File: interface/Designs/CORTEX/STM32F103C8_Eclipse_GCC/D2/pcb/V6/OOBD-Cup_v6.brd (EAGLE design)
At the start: 160 x 100 mm, 55 parts, among them IC1 PCA82C250T, IC2 78L05SMD, IC3 MC34063-SO, IC4 BTM-182, Q1 8MHz, T1 BC817, T2 BC817, T3 BC817, U1 STM32F10XTXU6

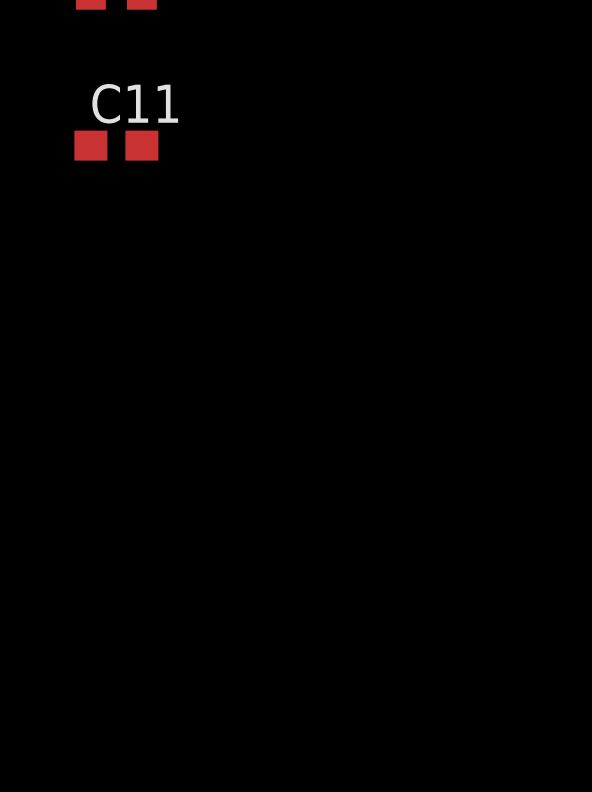
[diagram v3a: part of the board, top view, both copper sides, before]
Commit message: connect Relais to STM32 and add further EMC capacitor
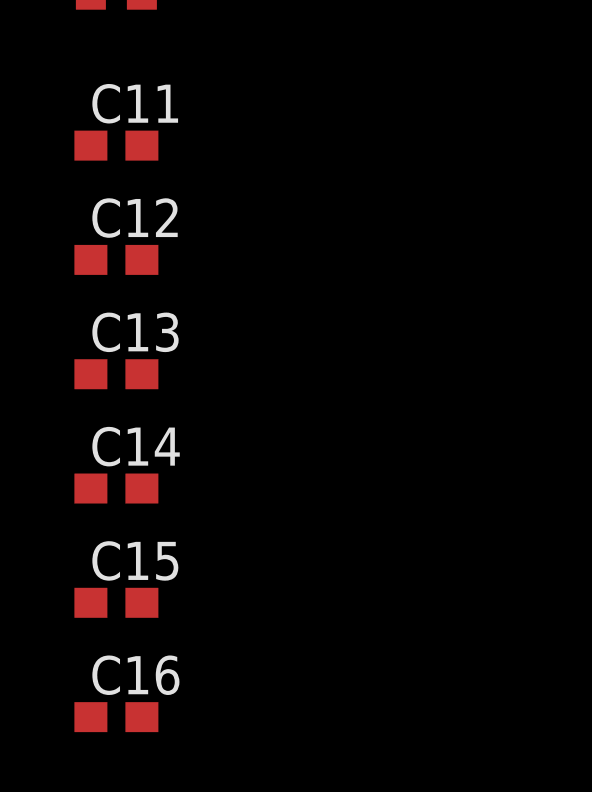
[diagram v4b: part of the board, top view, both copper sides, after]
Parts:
- added C12, C13, C14, C15, C16: 100nF, resistor:C0603
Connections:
- net +3V3: now also C12.1, C13.1, C14.1, C15.1
- net +5V: now also C16.1
- net CAN_SW: now also U1.30
- net GND: now also C12.2, C13.2, C14.2, C15.2, C16.2
- net REL_DIAG: now also U1.16
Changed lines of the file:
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@@
 <element name="R21" library="resistor" package="R0603" value="27k" x="-91.44" y="-153.67"/>
 <element name="C11" library="resistor" package="C0603" value="" x="-91.44" y="-158.75"/>
+<element name="C12" library="resistor" package="C0603" value="100nF" x="-91.44" y="-162.56"/>
+<element name="C13" library="resistor" package="C0603" value="100nF" x="-91.44" y="-166.37"/>
+<element name="C14" library="resistor" package="C0603" value="100nF" x="-91.44" y="-170.18"/>
+<element name="C15" library="resistor" package="C0603" value="100nF" x="-91.44" y="-173.99"/>
+<element name="C16" library="resistor" package="C0603" value="100nF" x="-91.44" y="-177.8"/>
 </elements>
 <signals>
@@
 <contactref element="R21" pad="1"/>
 <contactref element="C11" pad="2"/>
+<contactref element="C13" pad="2"/>
+<contactref element="C14" pad="2"/>
+<contactref element="C12" pad="2"/>
+<contactref element="C15" pad="2"/>
+<contactref element="C16" pad="2"/>
+<wire x1="-90.59" y1="-158.75" x2="-90.59" y2="-162.56" width="0" layer="19" extent="1-1"/>
+<wire x1="-90.59" y1="-166.37" x2="-90.59" y2="-162.56" width="0" layer="19" extent="1-1"/>
+<wire x1="-90.59" y1="-170.18" x2="-90.59" y2="-166.37" width="0" layer="19" extent="1-1"/>
+<wire x1="-90.59" y1="-173.99" x2="-90.59" y2="-170.18" width="0" layer="19" extent="1-1"/>
+<wire x1="-90.59" y1="-177.8" x2="-90.59" y2="-173.99" width="0" layer="19" extent="1-1"/>
 <wire x1="-92.29" y1="-153.67" x2="-90.59" y2="-158.75" width="0" layer="19" extent="1-1"/>
 <wire x1="-92.29" y1="-140.97" x2="-92.29" y2="-153.67" width="0" layer="19" extent="1-1"/>
@@
 <contactref element="R17" pad="2"/>
 <contactref element="JP1" pad="1"/>
+<contactref element="C12" pad="1"/>
+<contactref element="C14" pad="1"/>
+<contactref element="C13" pad="1"/>
+<contactref element="C15" pad="1"/>
+<wire x1="-92.29" y1="-162.56" x2="-90.59" y2="-134.62" width="0" layer="19" extent="1-1"/>
+<wire x1="-92.29" y1="-166.37" x2="-92.29" y2="-162.56" width="0" layer="19" extent="1-1"/>
+<wire x1="-92.29" y1="-170.18" x2="-92.29" y2="-166.37" width="0" layer="19" extent="1-1"/>
+<wire x1="-92.29" y1="-173.99" x2="-92.29" y2="-170.18" width="0" layer="19" extent="1-1"/>
 <wire x1="-72.39" y1="-110.49" x2="-90.59" y2="-134.62" width="0" layer="19" extent="1-1"/>
 <wire x1="-57.15" y1="-111.76" x2="-72.39" y2="-110.49" width="0" layer="19" extent="1-1"/>
@@
 <contactref element="R8" pad="1"/>
 <contactref element="R9" pad="2"/>
+<contactref element="U1" pad="16"/>
 <wire x1="-53.76" y1="-49.53" x2="-66.89" y2="-49.53" width="0" layer="19" extent="1-1"/>
+<wire x1="-28.21" y1="40.48" x2="-53.76" y2="-49.53" width="0" layer="19" extent="1-1"/>
 </signal>
 <signal name="N$20">
@@
 <signal name="CAN_SW">
 <contactref element="R7" pad="1"/>
+<contactref element="U1" pad="30"/>
+<wire x1="-28.21" y1="45.88" x2="-60.54" y2="-49.53" width="0" layer="19" extent="1-1"/>
 </signal>
 <signal name="N$27">
@@
 <contactref element="IC2" pad="1"/>
 <contactref element="C8" pad="1"/>
+<contactref element="C16" pad="1"/>
 <wire x1="-81.915" y1="-110.55" x2="-83.4" y2="-119.38" width="0" layer="19" extent="1-1"/>
 <wire x1="-69.215" y1="-79.2734" x2="-81.915" y2="-110.55" width="0" layer="19" extent="1-1"/>
+<wire x1="-92.29" y1="-177.8" x2="-83.4" y2="-119.38" width="0" layer="19" extent="1-1"/>
 <wire x1="-34.925" y1="2.0066" x2="-69.215" y2="-79.2734" width="0" layer="19" extent="1-1"/>
 </signal>

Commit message: add missing parts and doe last modification for first prototypes/batch
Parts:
- added C17: 47µ/35V, cap-master:SV-D
- added C18: 100nF, rcl:C0603K
- added C19: 100nF, resistor:C0603
- added C20, C21: 100n, resistor:C0603
- added IC5: 78L05SMD, linear:SO08
- added R22, R23, R24: 1R, rcl:R0805
- added R25: 5k6, rcl:R0603
- added T4: BC817, transistor:SOT23
- C1: value 1µF -> 100nF; device rcl:C0603K -> resistor:C0603
- C10: value 15p -> 100nF
- C11: value (none) -> 100nF
- C12: value 100nF -> 1µF; device resistor:C0603 -> rcl:C0603K
- C14: value 100nF -> 220µF; device resistor:C0603 -> rc-master:C6032-TE-C
- C15: value 100nF -> 220pF; device resistor:C0603 -> rcl:C0603K
- C2: value 220µF -> 100nF; device rc-master:C6032-TE-C -> rcl:C0603
- C3: value 220pF -> 15p; device rcl:C0603K -> resistor:C0603
- C4: value 47µ/35V -> 15p; device cap-master:SV-D -> resistor:C0603
- C5: device rcl:C0603K -> rcl:C0603
- C6: value 100n -> 100nF; device resistor:C0603 -> rcl:C0603
- C7: value 10nF -> 100nF
- C8: value 100n -> 100nF
- C9: value 15p -> 10nF
- D2: value B140 -> BAS40; device diode:SMB -> diode:SOT23
- D3: value BAS40 -> B140; device diode:SOT23 -> diode:SMB
- IC1: value PCA82C250T -> 24LC16; device can:SO08 -> microchip:SOT23-5L
- IC2: value 78L05SMD -> BTM-182; device linear:SO08 -> BTM182:BTM-182
- IC3: value MC34063-SO -> PCA82C250T; device mc34063:SO8 -> can:SO08
- IC4: value BTM-182 -> MC34063-SO; device BTM182:BTM-182 -> mc34063:SO8
- L1: value 47uH -> 100uH
- L2: value 47µH -> 100µH
- LED1: value Blue -> Rt/Gr; device led:U57X32 -> led:DUOLED2X5
- LED2: value Rt/Gr -> Blue; device led:DUOLED2X5 -> led:U57X32
- R1: value 82R -> 130k; device rcl:R0603 -> resistor:R0603
- R11: value 3k3 -> 4k7; device rcl:R0603 -> resistor:R0603
- R12: value 1R -> 510R; device rcl:R0805 -> rcl:R0603
- R13, R14: value 1R -> 4k7; device rcl:R0805 -> rcl:R0603
- R15: value 5k6 -> 4k7
- R16: value 120R -> 4k7; device resistor:R0603 -> rcl:R0603
- R17: value 10k -> 180k; device resistor:R0603 -> rcl:R0603
- R18: value 510R -> 47k; device resistor:R0603 -> rcl:R0603
- R19: value 10k -> 120R
- R2: value 4k7 -> 27k; device rcl:R0603 -> resistor:R0603
- R20: value 130k -> 510R
- R21: value 27k -> 3k3; device resistor:R0603 -> rcl:R0603
- R3: value 82R -> 10k; device rcl:R0603 -> resistor:R0603
- R4: value 4k7 -> 10k; device rcl:R0603 -> resistor:R0603
- R7: value 4k7 -> 82R
- R8: value 180k -> 82R
- R9: value 47k -> 4k7; device rcl:R0603 -> resistor:R0603
- moved R11 314.9 mm to (-100.3, -232.4)
- moved C2 288.0 mm to (-100.3, -227.3)
- moved C5 282.8 mm to (-91.4, -204.5)
- moved R12 260.8 mm to (-91.4, -195.6)
- moved R10 259.6 mm to (-91.4, -182.9)
- moved C15 251.7 mm to (-34.3, 71.1)
- moved C12 239.7 mm to (-38.1, 71.1)
- moved R21 236.9 mm to (-16.5, 71.1)
- moved C1 236.0 mm to (-91.4, -158.8)
- moved IC1 235.2 mm to (-100.3, -221.0)
- moved T1 234.1 mm to (-90.2, -189.2)
- moved C14 230.6 mm to (-25.4, 50.8)
- moved R2 223.7 mm to (-91.4, -153.7)
- moved R4 212.6 mm to (-91.4, -141.0)
- moved R3 211.6 mm to (-91.4, -134.6)
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- renumbered IC$2 to IC$1, JP3 to JP2
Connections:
- removed net RX_L: IC$1.2
- new net N$17: R10.2, T1.1
- new net N$19: IC1.1, R9.1, U1.33
- new net N$21: IC1.3, R11.1, U1.34
- new net N$8: R10.1, U1.11
- net +12V: now also C17.+, C18.1, C20.1, D3.C, IC4.6, IC5.8, LED2.A, R1.2, R22.2, R23.2, R24.2; no longer C4.+, C5.1, C6.1, D2.C, IC2.8, IC3.6, LED1.A, R12.2, R13.2, R14.2, R20.2
- net +3V3: now also C10.1, C11.1, C14.+, C16.1, C2.1, C5.1, C6.1, IC1.4, IC2.P$14, IC2.P$16, R11.2, R25.2, R3.2, R9.2; no longer C1.1, C14.1, C15.1, C2.+, IC4.P$14, IC4.P$16, R15.2, R17.2
- net +5V: now also C19.1, C21.1, C7.1, IC3.3, IC5.1; no longer C16.1, C8.1, IC1.3, IC2.1
- net BOOT0: now also R4.2; no longer R19.2
- net BTM_RX: now also IC2.P$10; no longer IC4.P$10
- net BTM_TX: now also IC2.P$9; no longer IC4.P$9
- net BT_RES-: now also IC2.P$21, U1.29; no longer IC4.P$21
- net BUZZER: now also R14.1; no longer R10.1
- net CAN-RXD: now also IC3.4, U1.23; no longer IC1.4
- net CAN-TXD: now also IC3.1, U1.24; no longer IC1.1
- net CAN_SW: now also R16.1; no longer R7.1
- net GND: now also C10.2, C14.-, C17.-, C18.2, C19.2, C2.2, C20.2, C21.2, C3.1, C4.1, C9.2, D2.1, IC2.P$15, IC3.2, IC3.8, IC4.4, IC5.2, IC5.3, IC5.6, IC5.7, LED1.K, R18.1, R2.1, R21.2, R4.1, T4.2; no longer C10.1, C14.2, C2.-, C3.2, C4.-, C9.1, D3.1, IC1.8, IC2.2, IC2.3, IC2.6, IC2.7, IC3.4, IC4.P$15, LED2.K, R11.2, R19.1, R21.1, R9.1
- net K-LINE: now also C9.1, R20.1; no longer C7.1, R18.1
- net L-LINE: now also R12.1, T1.3; no longer IC$1.8
- net LED1: now also R8.1; no longer R3.1
- net LED2: now also R7.1; no longer R1.1
- net LED_BLUE: now also R13.1; no longer R2.1
- net N$1: now also C4.2; no longer C10.2
- net N$10: now also R15.2, T2.3; no longer R4.2, T1.3
- net N$11: now also C15.1, IC4.3; no longer C3.1, IC3.3
- net N$12: now also IC4.1, IC4.7, IC4.8, R22.1, R23.1, R24.1; no longer IC3.1, IC3.7, IC3.8, R12.1, R13.1, R14.1
- net N$13: now also IC4.5, R21.1, R25.1; no longer IC3.5, R11.1, R15.1
- net N$14: now also D2.3, IC4.2; no longer D3.3, IC3.2
- net N$15: now also C1.1, R1.1, R2.2; no longer C11.1, R20.1, R21.2
- net N$16: now also R19.1; no longer R16.1
- net N$2: now also C3.2; no longer C9.2
- net N$20: now also R16.2, T4.1; no longer R7.2, T2.1
- net N$24: now also R14.2; no longer R10.2
- net N$27: now also R17.2, T4.3; no longer R8.2, T2.3
- net N$3: now also IC3.6; no longer IC1.6
- net N$4: now also LED1.AR, R8.2; no longer LED2.AR, R3.2
- net N$5: now also IC3.7, R19.2; no longer IC1.7, R16.2
- net N$6: now also LED1.AG, R7.2; no longer LED2.AG, R1.2
- net N$7: now also LED2.K, R15.1; no longer LED1.K, R4.1
- net N$9: now also R13.2, T2.1; no longer R2.2, T1.1
- net REL_DIAG: now also R17.1, R18.2; no longer R8.1, R9.2
- net RESET-: now also R3.1; no longer R17.1
- net VBAT: now also C8.1, D3.A, R12.2, R20.2; no longer D2.A, R18.2

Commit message: add necessary modifications for switching regulator MC34063
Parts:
- D2: value BAS40 -> B140; device diode:SOT23 -> diode:SMB
- L1: value 100uH -> 47uH
- L2: value 100µH -> 47µH
- moved R9 315.1 mm to (-20.3, 66.0)
- moved C2 303.6 mm to (-44.5, 71.1)
- moved R11 293.5 mm to (-61.0, 58.4)
- moved C8 285.5 mm to (-39.4, 66.0)
- moved C7 281.7 mm to (-33.0, 66.0)
- moved C5 278.4 mm to (-52.1, 71.1)
- moved C6 273.6 mm to (-59.7, 71.1)
- moved IC1 270.8 mm to (-40.6, 43.2)
- moved R10 268.3 mm to (-26.7, 77.5)
- moved R12 267.9 mm to (-66.0, 71.1)
- moved C19 244.7 mm to (-71.1, 66.0)
- moved C16 241.5 mm to (-64.8, 66.0)
- moved C11 239.5 mm to (-52.1, 66.0)
- moved C10 236.9 mm to (-45.7, 66.0)
- moved T1 234.9 mm to (-48.3, 41.9)
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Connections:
- net GND: now also D2.A; no longer D2.1
- net N$14: now also D2.C; no longer D2.3

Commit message: add latest modification for optional WLAN-Interface
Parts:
- added JP3: (no value), jumper:JP1
- JP1: device jumper:JP4Q -> jumper:JP5Q
- JP2: value (none) -> ext. WLAN; device jumper:JP1 -> jumper:JP3Q
- moved JP2 76.1 mm to (-78.7, -3.81)
- moved JP1 49.6 mm to (-66.0, -5.08)
- moved T2 7.62 mm to (-63.5, 41.9)
- moved T3 7.62 mm to (-55.9, 41.9)
- moved R13 5.08 mm to (-36.8, 77.5)
- moved R14 5.08 mm to (-31.8, 77.5)
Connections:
- removed net N$4: LED1.AR, R8.2
- removed net N$6: LED1.AG, R7.2
- removed net N$7: LED2.K, R15.1
- new net 3V3_BTM182: C5.1, C6.1, IC2.P$14, IC2.P$16, JP1.9
- new net LED1_GR: JP2.1, LED1.AG, R7.2
- new net LED1_RT: JP2.3, LED1.AR, R8.2
- new net LED2_BL: JP2.4, LED2.K, R15.1
- net +12V: now also JP2.2
- net +3V3: now also JP1.10, JP1.8; no longer C5.1, C6.1, IC2.P$14, IC2.P$16, JP1.1
- net BOOT0: now also JP1.7; no longer JP1.2
- net BTM_RX: now also JP1.1; no longer JP1.8
- net BTM_TX: now also JP1.3; no longer JP1.6
- net BUZZER: now also R13.1; no longer R14.1
- net GND: now also JP1.6, JP2.5; no longer JP1.3
- net LED_BLUE: now also R14.1; no longer R13.1
- net N$10: now also T3.3; no longer T2.3
- net N$16: now also JP3.2; no longer JP2.2
- net N$23: now also T2.3; no longer T3.3
- net N$3: now also JP3.1; no longer JP2.1
- net RESET-: now also JP1.5; no longer JP1.4
- net STM_RXD: now also JP1.4; no longer JP1.5
- net STM_TXD: now also JP1.2; no longer JP1.7
- net VBAT: now also JP2.6
